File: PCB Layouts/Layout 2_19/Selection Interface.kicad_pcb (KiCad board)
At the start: 4 copper layers, 107.5 x 80 mm, 86 parts

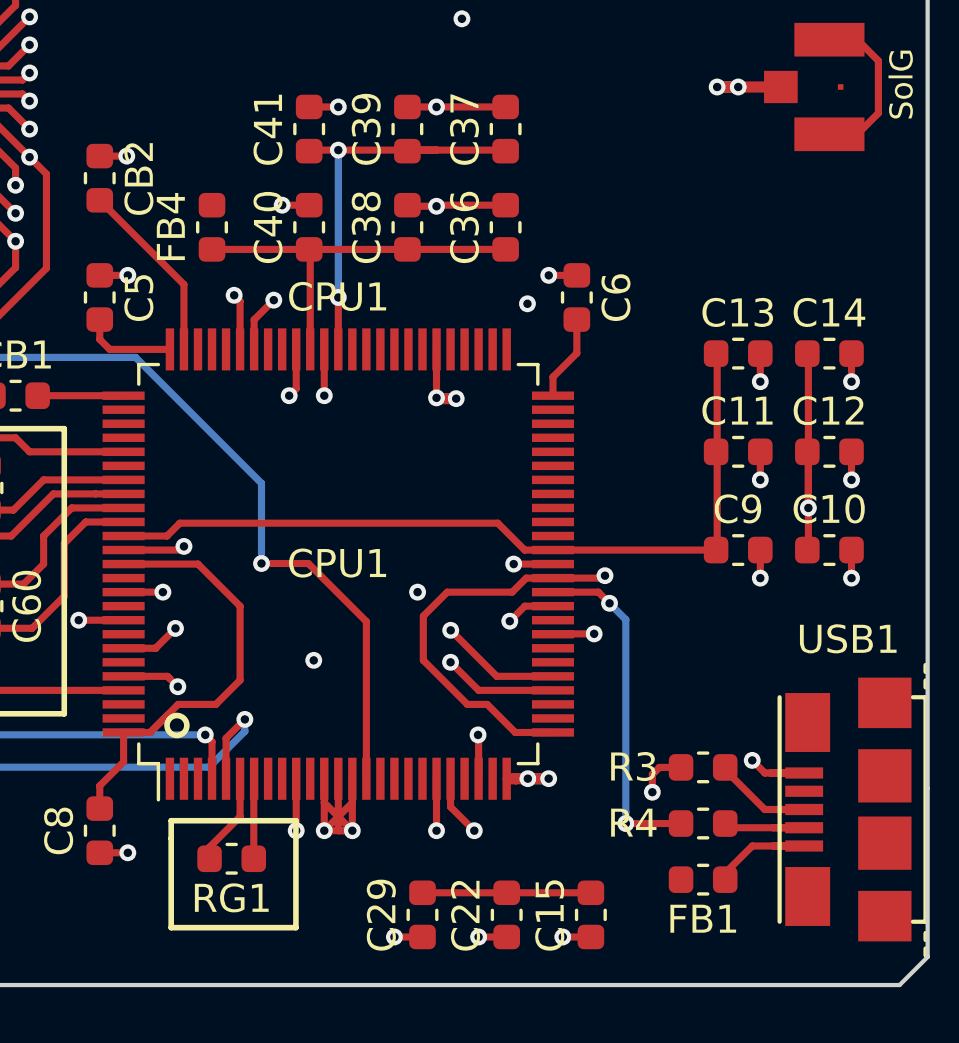
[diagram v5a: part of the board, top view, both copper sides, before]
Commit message: In Layout 2_19, added SMD capacitor for the gate signal
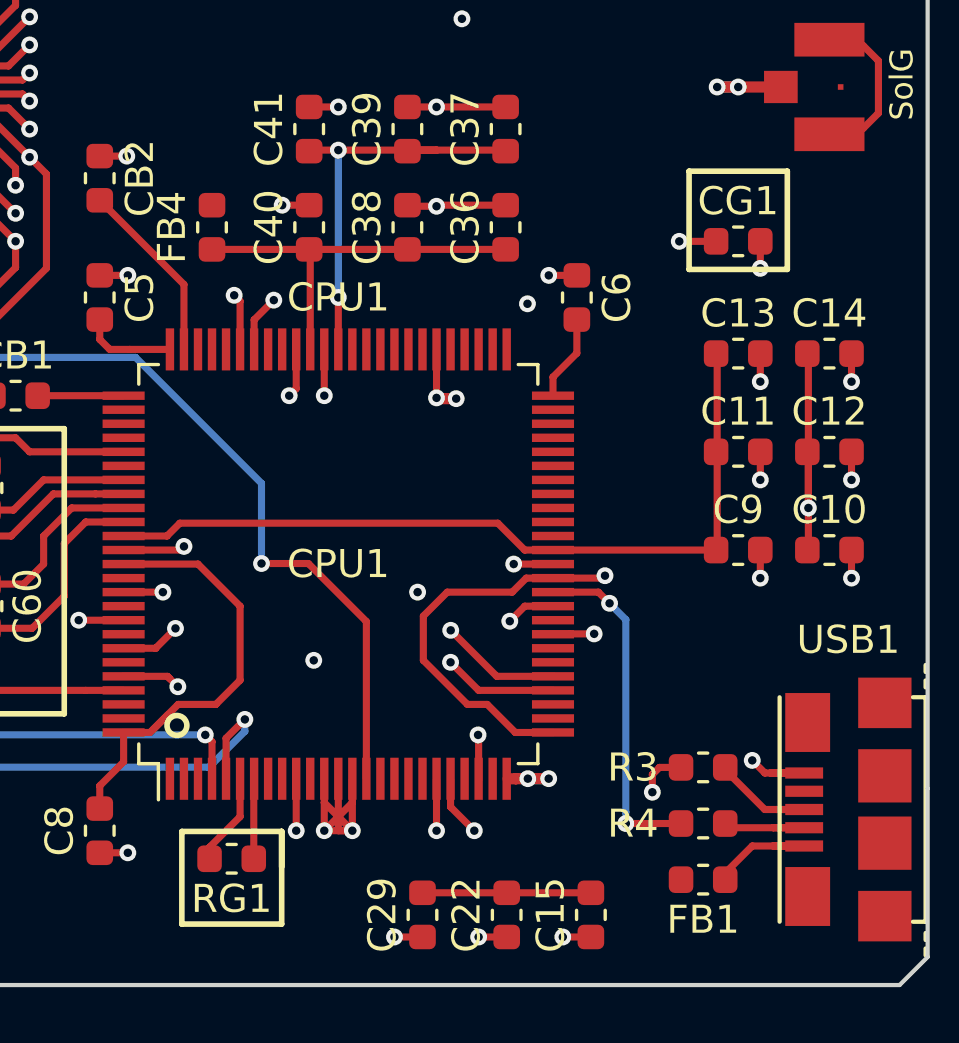
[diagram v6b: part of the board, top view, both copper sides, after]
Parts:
- added CG1: 1uF, Capacitor_SMD:C_0603_1608Metric, F.Cu at (253.2, 123.5)
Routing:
- net Gate: track 57.2 -> 58.5 mm, vias 4 -> 5
- net GND: track 429.0 -> 430.0 mm, vias 164 -> 165
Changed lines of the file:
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@@
   (general
     (thickness 1.6)
-    (drawings 400)
-    (tracks 3366)
+    (drawings 404)
+    (tracks 3372)
     (zones 0)
-    (modules 86)
+    (modules 87)
     (nets 197)
   )
   (page A4)
   (layers
-    (0 F.Cu signal hide)
-    (1 In1.Cu signal hide)
-    (2 In2.Cu signal hide)
-    (31 B.Cu signal hide)
+    (0 F.Cu signal)
+    (1 In1.Cu signal)
+    (2 In2.Cu signal)
+    (31 B.Cu signal)
     (32 B.Adhes user)
     (33 F.Adhes user)
     (34 B.Paste user)
     (35 F.Paste user)
-    (36 B.SilkS user hide)
+    (36 B.SilkS user)
     (37 F.SilkS user)
     (38 B.Mask user)
@@
     (44 Edge.Cuts user)
     (45 Margin user)
-    (46 B.CrtYd user hide)
-    (47 F.CrtYd user hide)
-    (48 B.Fab user hide)
+    (46 B.CrtYd user)
+    (47 F.CrtYd user)
+    (48 B.Fab user)
     (49 F.Fab user)
   )
@@
     )
   )
+  (module Capacitor_SMD:C_0603_1608Metric (layer F.Cu)
+    (at 253.25 123.5)
+    (descr "Capacitor SMD 0603 (1608 Metric), square (rectangular) end terminal, IPC_7351 nominal, (Body size source: http://www.tortai-tech.com/upload/download/2011102023233369053.pdf), generated with kicad-footprint-generator")
+    (tags capacitor)
+    (attr smd)
+    (fp_text reference CG1 (at 0 -1.43) (layer F.SilkS)
+      (effects (font (size 1 1) (thickness 0.15)))
+    )
+    (fp_text value 1uF (at 0 1.43) (layer F.Fab)
+      (effects (font (size 1 1) (thickness 0.15)))
+    )
+    (fp_line (start -0.8 0.4) (end -0.8 -0.4) (layer F.Fab) (width 0.1))
+    (fp_line (start -0.8 -0.4) (end 0.8 -0.4) (layer F.Fab) (width 0.1))
+    (fp_line (start 0.8 -0.4) (end 0.8 0.4) (layer F.Fab) (width 0.1))
+    (fp_line (start 0.8 0.4) (end -0.8 0.4) (layer F.Fab) (width 0.1))
+    (fp_line (start -0.162779 -0.51) (end 0.162779 -0.51) (layer F.SilkS) (width 0.12))
+    (fp_line (start -0.162779 0.51) (end 0.162779 0.51) (layer F.SilkS) (width 0.12))
+    (fp_line (start -1.48 0.73) (end -1.48 -0.73) (layer F.CrtYd) (width 0.05))
+    (fp_line (start -1.48 -0.73) (end 1.48 -0.73) (layer F.CrtYd) (width 0.05))
+    (fp_line (start 1.48 -0.73) (end 1.48 0.73) (layer F.CrtYd) (width 0.05))
+    (fp_line (start 1.48 0.73) (end -1.48 0.73) (layer F.CrtYd) (width 0.05))
+    (fp_text user %R (at 0 0) (layer F.Fab)
+      (effects (font (size 0.4 0.4) (thickness 0.06)))
+    )
+    (pad 1 smd roundrect (at -0.7875 0) (size 0.875 0.95) (layers F.Cu F.Paste F.Mask) (roundrect_rratio 0.25)
+      (net 190 Gate))
+    (pad 2 smd roundrect (at 0.7875 0) (size 0.875 0.95) (layers F.Cu F.Paste F.Mask) (roundrect_rratio 0.25)
+      (net 1 GND))
+    (model ${KISYS3DMOD}/Capacitor_SMD.3dshapes/C_0603_1608Metric.wrl
+      (at (xyz 0 0 0))
+      (scale (xyz 1 1 1))
+      (rotate (xyz 0 0 0))
+    )
+  )
+  (gr_line (start 251.5 121) (end 251.5 124.5) (layer F.SilkS) (width 0.2))
+  (gr_line (start 255 121) (end 255 124.5) (layer F.SilkS) (width 0.2))
+  (gr_line (start 251.5 124.5) (end 255 124.5) (layer F.SilkS) (width 0.2))
+  (gr_line (start 233.426 144.526) (end 233.426 147.828) (layer F.SilkS) (width 0.2))
+  (gr_line (start 236.982 144.526) (end 233.426 144.526) (layer F.SilkS) (width 0.2))
+  (gr_line (start 236.982 147.828) (end 233.426 147.828) (layer F.SilkS) (width 0.2))
+  (gr_line (start 236.982 144.526) (end 236.982 147.828) (layer F.SilkS) (width 0.2))
+  (gr_line (start 236.982 145.796) (end 236.982 144.526) (layer F.SilkS) (width 0.2))
+  (gr_line (start 251.5 121) (end 255 121) (layer F.SilkS) (width 0.2))
   (gr_text 1k (at 175.895 101.092) (layer F.SilkS)
     (effects (font (size 1 1) (thickness 0.15)))
@@
     (effects (font (size 1 1) (thickness 0.15)))
   )
-  (gr_line (start 233.045 144.145) (end 233.045 144.78) (layer F.SilkS) (width 0.2))
-  (gr_line (start 237.49 144.145) (end 233.045 144.145) (layer F.SilkS) (width 0.2))
-  (gr_line (start 237.49 147.955) (end 237.49 144.145) (layer F.SilkS) (width 0.2))
-  (gr_line (start 233.045 147.955) (end 237.49 147.955) (layer F.SilkS) (width 0.2))
-  (gr_line (start 233.045 144.78) (end 233.045 147.955) (layer F.SilkS) (width 0.2))
   (gr_line (start 217.805 130.175) (end 229.235 130.175) (layer F.SilkS) (width 0.2))
   (gr_line (start 217.805 140.335) (end 217.805 130.175) (layer F.SilkS) (width 0.2))
@@
   (via (at 169.545 104.775) (size 0.6) (drill 0.3) (layers F.Cu B.Cu) (net 1))
   (segment (start 169.545 104.775) (end 167.005 104.775) (width 0.254) (layer B.Cu) (net 1))
+  (segment (start 254.0375 123.5) (end 254.0375 124.4625) (width 0.254) (layer F.Cu) (net 1))
+  (segment (start 254.0375 124.4625) (end 254.0375 124.4625) (width 0.254) (layer F.Cu) (net 1))
+  (via (at 254.0375 124.4625) (size 0.6) (drill 0.3) (layers F.Cu B.Cu) (net 1))
   (segment (start 246.65 139.5) (end 244 139.5) (width 0.254) (layer F.Cu) (net 2))
   (segment (start 244 139.5) (end 243 138.5) (width 0.254) (layer F.Cu) (net 2))
@@
   (segment (start 251.150002 140.009998) (end 248.514 142.646) (width 0.4) (layer In1.Cu) (net 190))
   (segment (start 249.75 102.17) (end 250.5 102.92) (width 0.4) (layer In1.Cu) (net 190))
-  (segment (start 251.150002 108.910002) (end 251.150002 140.009998) (width 0.4) (layer In1.Cu) (net 190))
+  (segment (start 251.150002 108.910002) (end 251.150002 123.5) (width 0.4) (layer In1.Cu) (net 190))
   (segment (start 250.5 108.26) (end 251.150002 108.910002) (width 0.4) (layer In1.Cu) (net 190))
   (segment (start 250.5 102.92) (end 250.5 108.26) (width 0.4) (layer In1.Cu) (net 190))
@@
   (segment (start 248.817 102.17) (end 248.817 102.17) (width 0.4) (layer F.Cu) (net 190))
   (via (at 248.817 102.17) (size 0.6) (drill 0.3) (layers F.Cu B.Cu) (net 190))
+  (segment (start 251.150002 123.5) (end 251.150002 140.009998) (width 0.4) (layer In1.Cu) (net 190))
+  (via (at 251.150002 123.5) (size 0.6) (drill 0.3) (layers F.Cu B.Cu) (net 190))
+  (segment (start 251.150002 123.5) (end 252.4625 123.5) (width 0.254) (layer F.Cu) (net 190))
   (segment (start 233.5 125.0375) (end 233.5 127.35) (width 0.254) (layer F.Cu) (net 194))
   (segment (start 230.5 122.0375) (end 233.5 125.0375) (width 0.254) (layer F.Cu) (net 194))

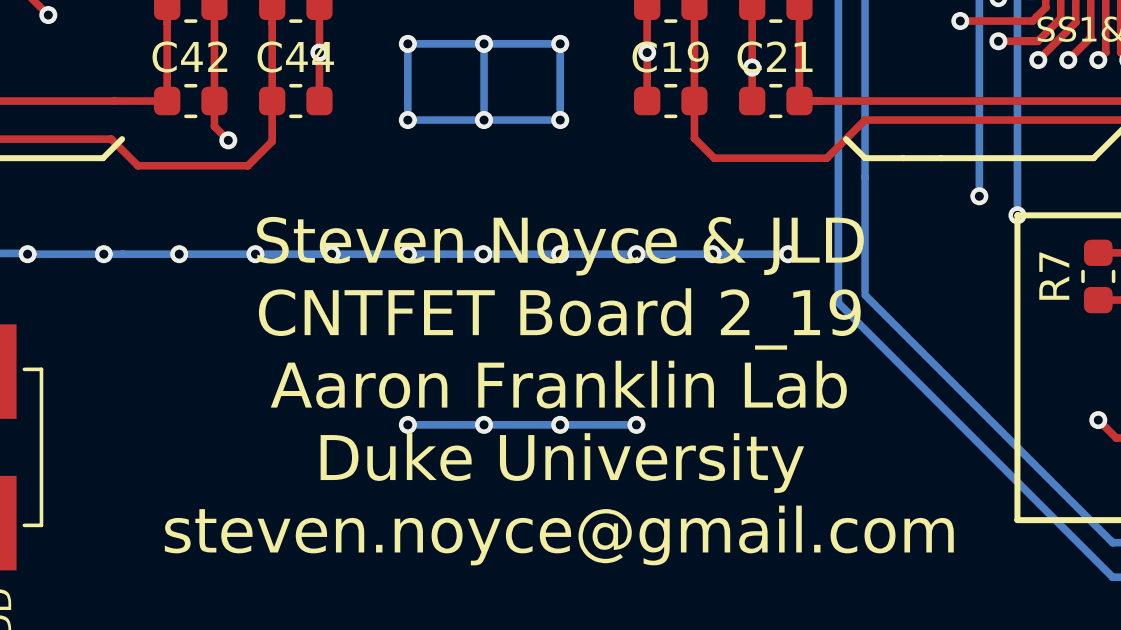
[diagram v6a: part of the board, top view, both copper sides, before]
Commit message: Updated recommended value of CG1 in Layout 2_19 based on my tests this afternoon
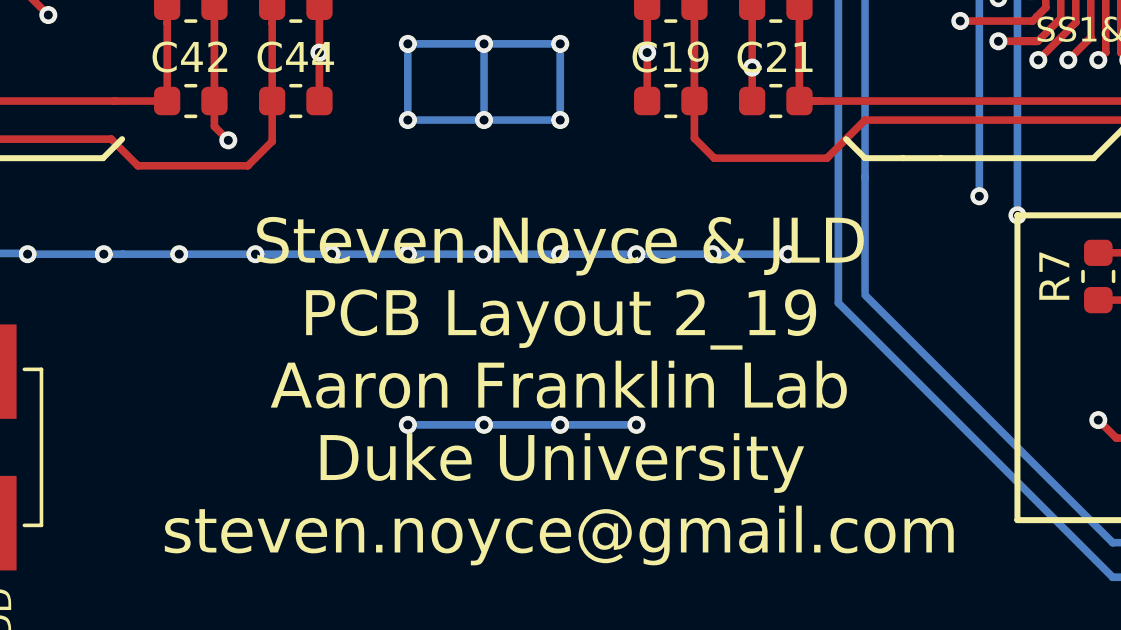
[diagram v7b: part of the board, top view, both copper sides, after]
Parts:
- CG1: value 1uF -> 1nF
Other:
- board text added: "Steven Noyce & JLD PCB Layout 2_19 Aaron Franklin Lab Duke University steven.noyce@gmail.com"
- board text removed: "Steven Noyce & JLD CNTFET Board 2_19 Aaron Franklin Lab Duke University steven.noyce@gmail.com"
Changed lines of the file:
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@@
     (44 Edge.Cuts user)
     (45 Margin user)
-    (46 B.CrtYd user)
-    (47 F.CrtYd user)
-    (48 B.Fab user)
+    (46 B.CrtYd user hide)
+    (47 F.CrtYd user hide)
+    (48 B.Fab user hide)
     (49 F.Fab user)
   )
@@
       (effects (font (size 1 1) (thickness 0.15)))
     )
-    (fp_text value 1uF (at 0 1.43) (layer F.Fab)
+    (fp_text value 1nF (at 3.25 0) (layer F.Fab)
       (effects (font (size 1 1) (thickness 0.15)))
     )
@@
     (effects (font (size 0.82 0.82) (thickness 0.16)))
   )
-  (gr_text "Steven Noyce & JLD\nCNTFET Board 2_19\nAaron Franklin Lab\nDuke University\nsteven.noyce@gmail.com" (at 202.565 135.89) (layer F.SilkS)
+  (gr_text "Steven Noyce & JLD\nPCB Layout 2_19\nAaron Franklin Lab\nDuke University\nsteven.noyce@gmail.com" (at 202.565 135.89) (layer F.SilkS)
     (effects (font (size 1.5 1.5) (thickness 0.3)))
   )

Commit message: Small tweaks to PCB Layout 2_19
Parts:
- CG1: value 1nF -> 1pF
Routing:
- net I2C0_SDA: track 194.1 -> 193.2 mm
- net GND: track 430.0 -> 429.3 mm
